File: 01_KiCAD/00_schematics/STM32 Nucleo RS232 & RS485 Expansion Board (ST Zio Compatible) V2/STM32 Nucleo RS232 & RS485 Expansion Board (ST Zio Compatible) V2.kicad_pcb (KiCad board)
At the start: 4 copper layers, 70 x 133.4 mm, 190 parts, among them CN10 Conn_02x17_Odd_Even, CN7 Conn_02x10_Odd_Even, CN8 Conn_02x08_Odd_Even, CN9 Conn_02x15_Odd_Even, IC1 REG103GA-A, J1 1190299, J10 DIR, J11 TERM_TX, J12 TERM_RX, J13 SLR, J2 CONN D-SUB PLUG 9POS TH, J3 TCVR_PWR, J4 TX_LED, J5 RX_LED, J6 SW_ENA, J7 MODE0, J8 MODE1, J9 MODE2, Q1 BSS84, Q2 BSS84, U1 TPS2117DRLR, U10 SN74LVC2G14DBV, U11 SN74LVC2G14DBV, U2 THVD4431RHAR, U3 SN74LVC2G14DBV, U4 SN74LVC245ADBR, U5 SN74LVC2G14DBV, U6 SN74LVC2G14DBV, U7 SN74LVC2G14DBV, U8 SN74LVC2G14DBV, U9 SN74LVC2G14DBV

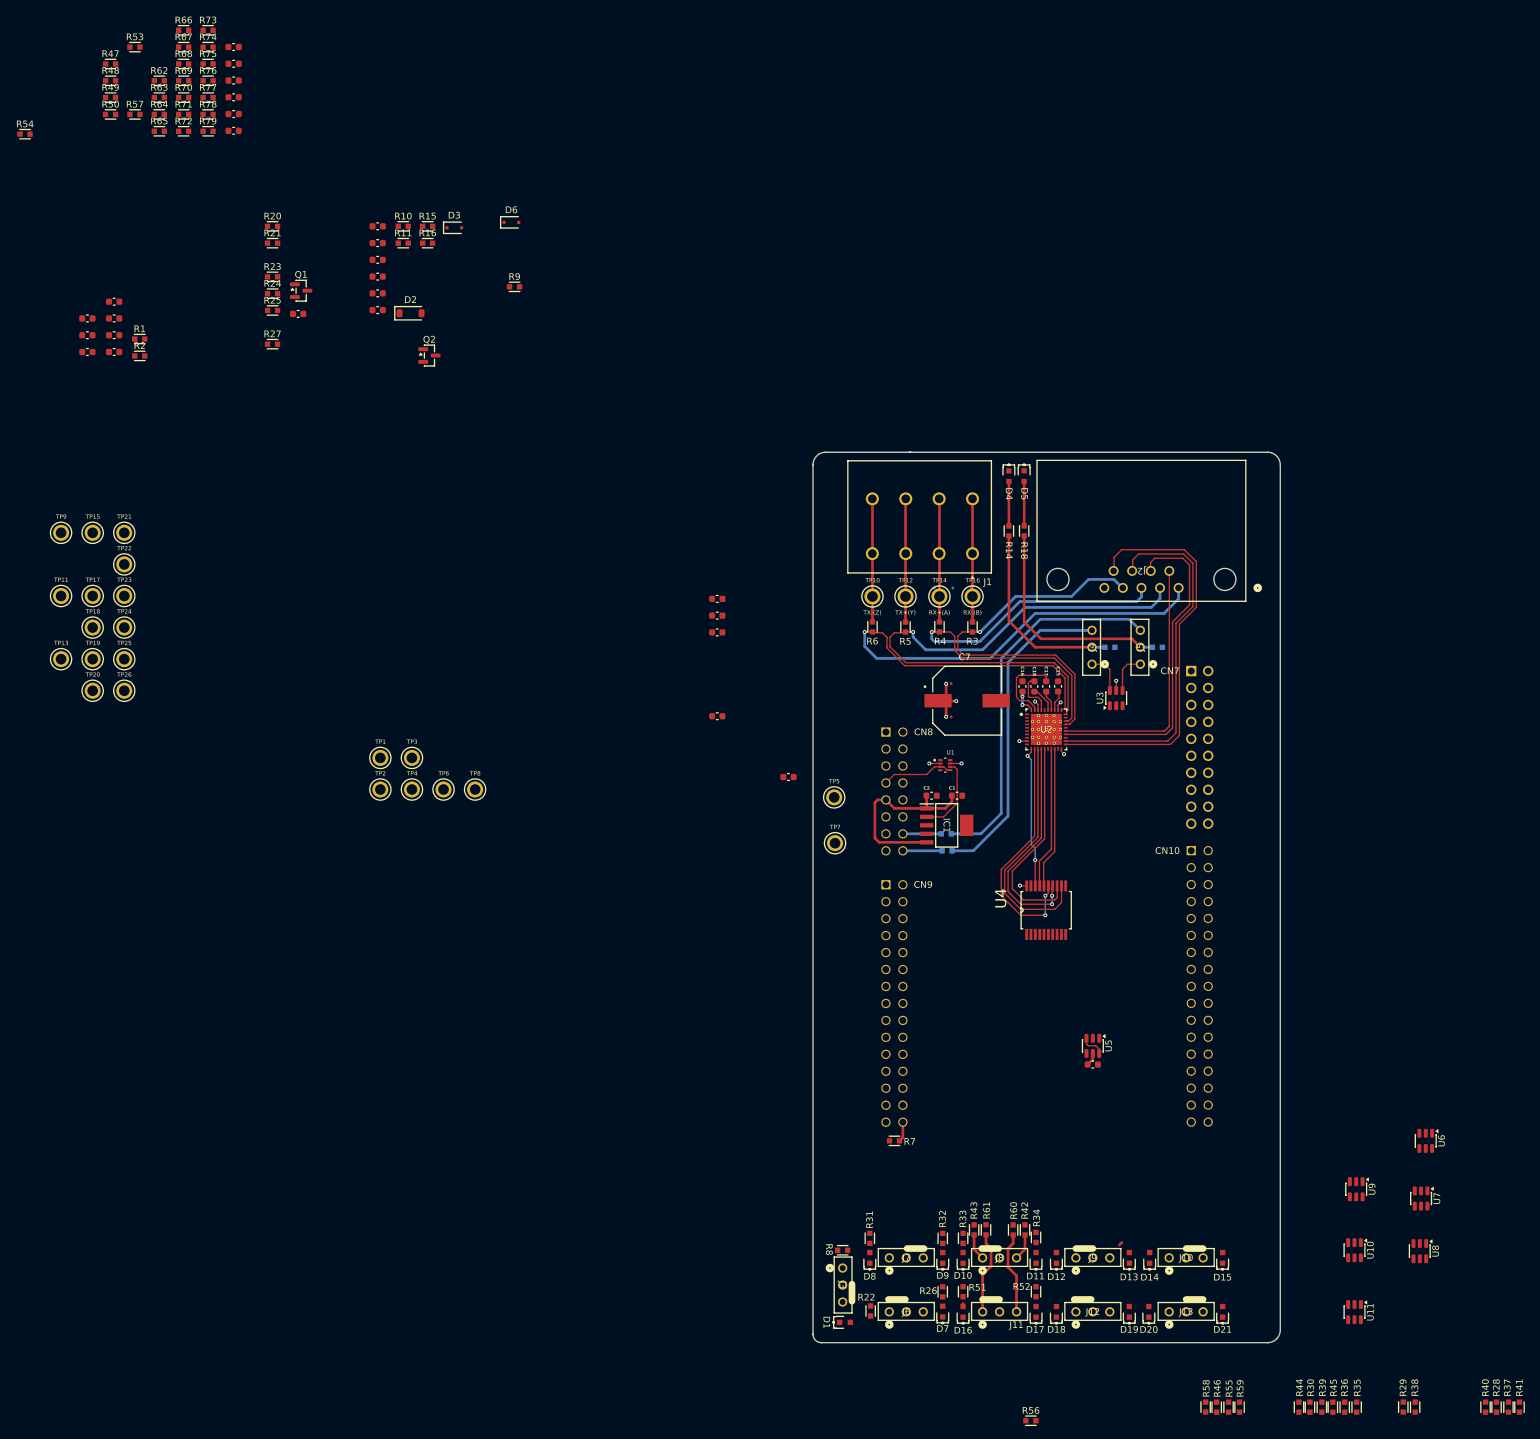
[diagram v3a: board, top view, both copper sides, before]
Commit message: Changed schmitt trigger
changed the schmitt trigger for hex-schmitt trigger variant to simpify design and reduce components
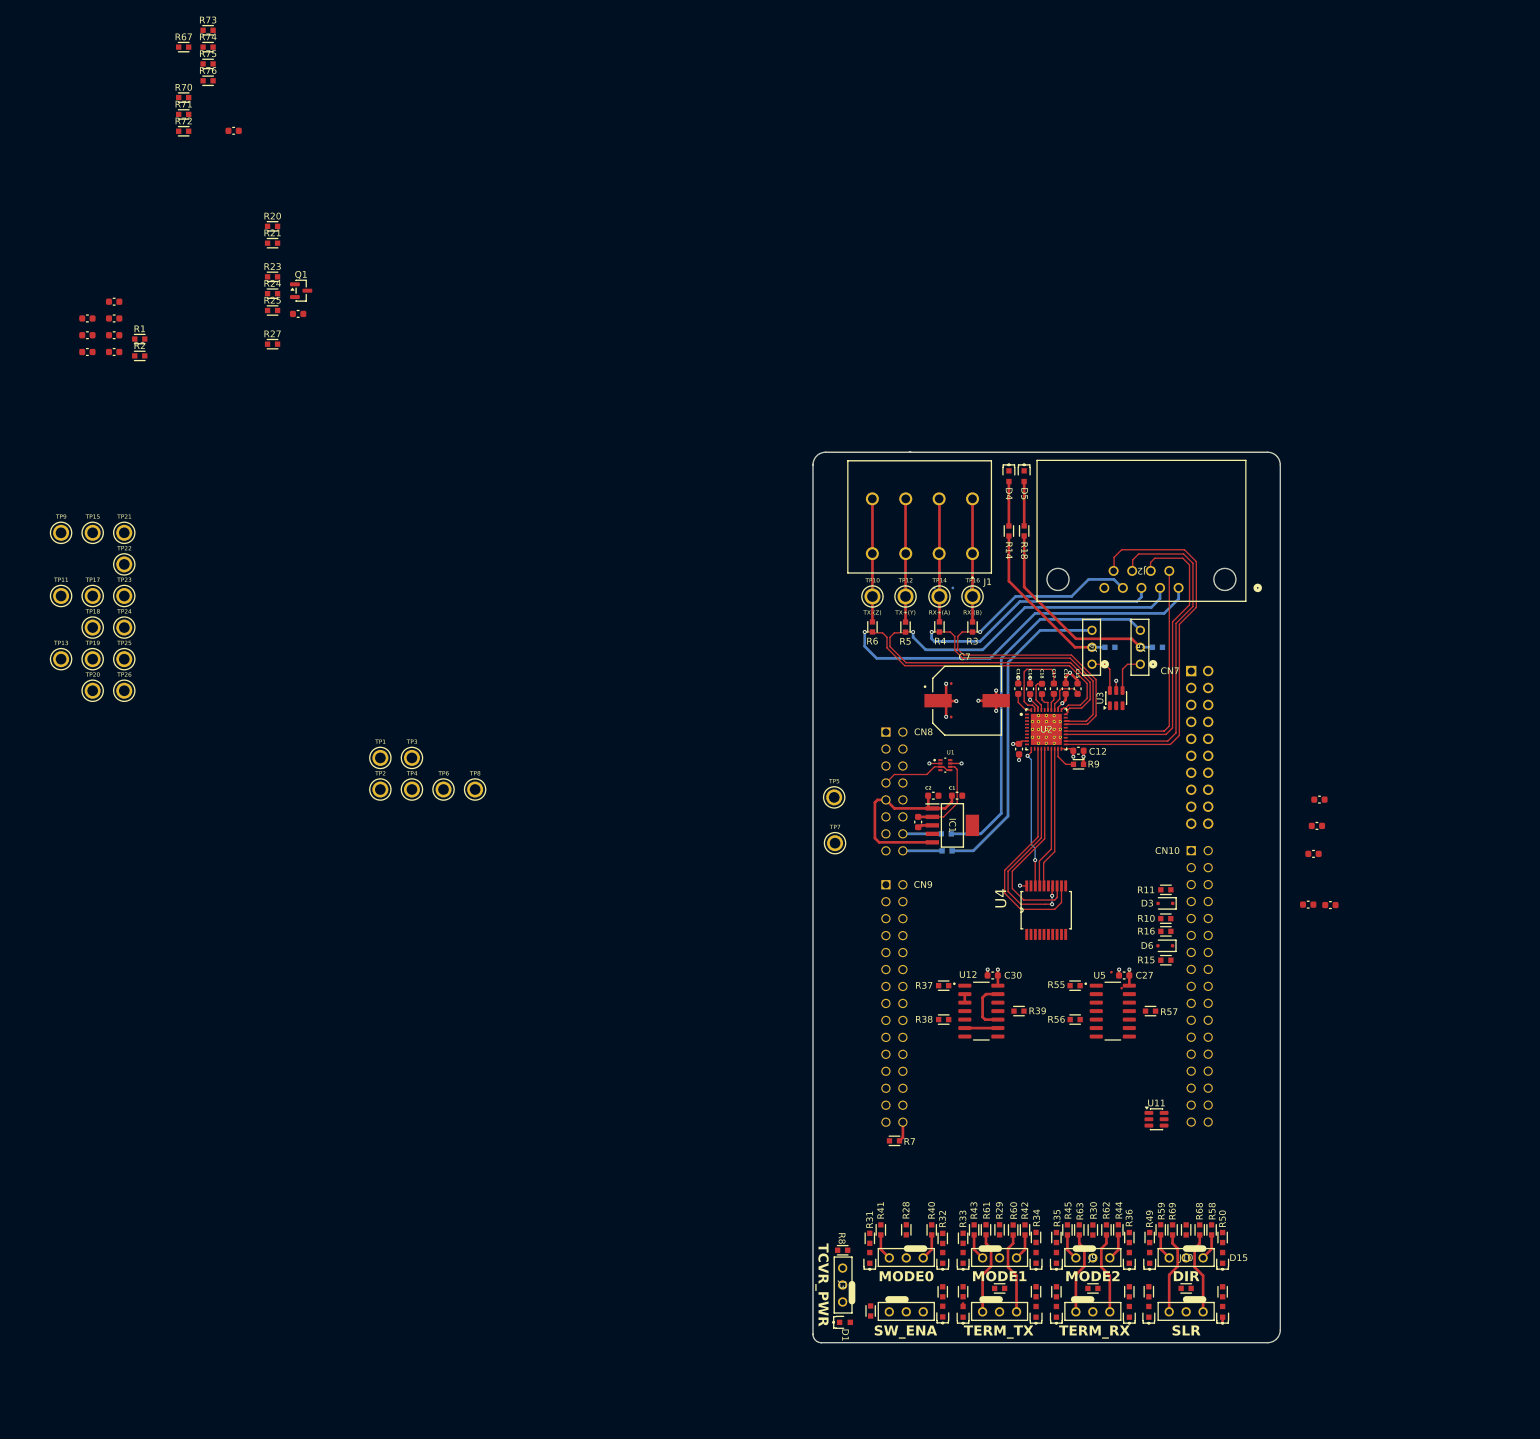
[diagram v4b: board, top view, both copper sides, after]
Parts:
- removed C23, C28, C29, C31, C32: 100nF, PCM_SparkFun-Capacitor:C_0603_1608Metric
- removed D2: 1N4148W, Diode_SMD:D_SOD-123
- removed Q2: BSS84, Package_TO_SOT_SMD:SOT-23
- removed R77: 10K, PCM_fab:R_0603
- removed R78: 3K3, PCM_fab:R_0603
- removed R79: 1K, PCM_fab:R_0603
- removed U10, U6, U7, U8, U9: SN74LVC2G14DBV, Package_TO_SOT_SMD:SOT-23-6
- added U12: SN74LVC14ADR, SN74LVC14ADR:SOIC127P600X175-14N, F.Cu at (62.0, 120.5)
- U5: value SN74LVC2G14DBV -> SN74LVC14ADR; footprint Package_TO_SOT_SMD:SOT-23-6 -> SN74LVC14ADR:SOIC127P600X175-14N
- moved R66 244.7 mm to (98.2, 162.6), turned to -90 degrees
- moved R54 239.6 mm to (84.2, 162.6), turned to -90 degrees
- moved R50 236.7 mm to (98.2, 154.4), turned to -90 degrees
- moved R64 233.6 mm to (92.7, 162.1), turned to 180 degrees
- moved R48 233.1 mm to (78.8, 162.1), turned to 180 degrees
- moved R53 231.9 mm to (73.3, 162.6), turned to 90 degrees
- moved R68 231.6 mm to (94.7, 153.3), turned to -90 degrees
- moved R49 231.0 mm to (87.2, 154.4), turned to 90 degrees
- moved R65 228.4 mm to (87.1, 162.5), turned to 90 degrees
- moved R69 227.0 mm to (90.7, 153.3), turned to -90 degrees
- moved R47 226.6 mm to (64.8, 162.1), turned to 180 degrees
- moved R62 223.0 mm to (80.8, 153.3), turned to -90 degrees
- moved R63 218.5 mm to (76.7, 153.3), turned to -90 degrees
- moved R57 202.9 mm to (87.4, 120.5), turned to 180 degrees
- moved C30 175.7 mm to (63.7, 115.2), turned to 180 degrees
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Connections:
- R37 pad 2: Net-(U5-1A) -> Net-(U12A-1A)
- R55 pad 2: Net-(U8-1A) -> Net-(U5A-1A)
- R56 pad 2: Net-(U9-1A) -> Net-(U5C-3A)
- R57 pad 2: Net-(U10-1A) -> Net-(U5E-5A)
- U5 pad 1: Net-(U5-1A) -> Net-(U5A-1A)
- U5 pad 2: GND -> Net-(D14-K)
- U5 pad 3: Net-(D8-K) -> Net-(D14-K)
- U5 pad 4: Net-(D9-K) -> Net-(D15-K)
- U5 pad 5: 3V3_SYS -> Net-(U5C-3A)
- U5 pad 6: Net-(D8-K) -> Net-(D16-K)
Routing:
- net DIR: track 36.5 -> 0.00 mm, vias 2 -> 0
- net GND: track 0.00 -> 18.4 mm, vias 0 -> 10
- net Net-(J13-Pin_1): track 0.00 -> 12.4 mm
- net Net-(J12-Pin_1): track 0.00 -> 12.4 mm
- net Net-(J13-Pin_3): track 0.00 -> 12.3 mm
- net Net-(J12-Pin_3): track 0.00 -> 12.3 mm
- net 3V3_SYS: track 20.3 -> 28.6 mm, vias 11 -> 13
- net Net-(D12-K): track 0.00 -> 7.86 mm
- net /RS232 & RS485 Tranceiver/RX-: track 58.4 -> 64.2 mm
- net /RS232 & RS485 Tranceiver/RX+: track 69.2 -> 75.0 mm
- net /RS232 & RS485 Tranceiver/TX+: track 82.8 -> 88.1 mm
- net /RS232 & RS485 Tranceiver/TX-: track 94.2 -> 99.5 mm
- net Net-(D10-K): track 0.00 -> 4.95 mm
- net /RS232 & RS485 Tranceiver/THVD_SHDN_N: track 0.00 -> 3.97 mm
- net Net-(J9-Pin_3): track 0.00 -> 3.97 mm
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
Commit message: Updated PCB
Updated PCB with components layout and routing tracks.
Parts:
- R12, R13, R17, R19: moved to F.Cu
- moved C33 214.2 mm to (99.0, 142.6)
- moved C22 40.9 mm to (82.3, 68.7), turned to 90 degrees
- moved C24 38.2 mm to (88.5, 76.5), turned to 90 degrees
- moved C25 38.0 mm to (85.5, 76.5), turned to -90 degrees
- moved C20 34.3 mm to (80.6, 76.5), turned to 90 degrees
- moved C21 32.9 mm to (83.7, 76.5), turned to -90 degrees
- moved R16 32.2 mm to (87.0, 76.5), turned to 90 degrees
- moved R11 27.0 mm to (82.2, 76.4), turned to 90 degrees
- moved U11 8.85 mm to (94.9, 142.6)
- moved R19 3.81 mm to (56.9, 97.8)
- moved R12 3.43 mm to (56.9, 99.9)
- moved R17 2.10 mm to (89.3, 64.1), turned to -90 degrees
- moved R13 2.05 mm to (82.0, 64.1), turned to 90 degrees
- moved D3 1.91 mm to (89.5, 106.3)
- moved R10 1.91 mm to (89.5, 108.6)
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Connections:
- net Net-(D6-A) renamed /Rx & Tx LED/RX_RC
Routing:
- net /RS232 & RS485 Tranceiver/THVD_SHDN_N: track 3.97 -> 115.7 mm, vias 0 -> 1
- net Net-(D8-K): track 1.27 -> 53.7 mm
- net Net-(J3-Pin_3): track 0.00 -> 29.6 mm
- net Net-(D21-K): track 0.77 -> 26.1 mm
- net ARDUINO_5V: track 29.9 -> 53.3 mm
- net 3V3_SYS: track 28.6 -> 49.3 mm, vias 13 -> 34
- net Net-(D1-A): track 0.00 -> 13.1 mm
- net GND: track 18.4 -> 29.9 mm, vias 10 -> 22
- net L3-TXD: track 0.00 -> 7.50 mm
- net L2-RXD: track 0.00 -> 6.16 mm
- net Net-(J4-Pin_3): track 48.1 -> 52.4 mm, vias 0 -> 1
- net Net-(J5-Pin_2): track 30.6 -> 34.9 mm
- net Net-(J5-Pin_3): track 56.0 -> 59.9 mm, vias 0 -> 1
- net Net-(J6-Pin_1): track 0.00 -> 3.05 mm
- net Net-(D3-K): track 0.00 -> 3.03 mm
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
